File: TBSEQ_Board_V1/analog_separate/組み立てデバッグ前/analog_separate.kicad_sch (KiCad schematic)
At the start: 0 parts

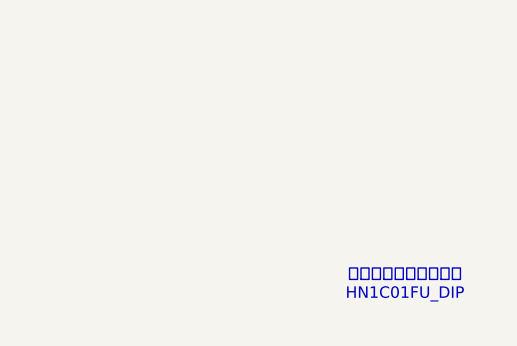
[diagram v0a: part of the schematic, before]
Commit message: analog_separate fix
実装してバグを修正
・VR6以外のボリュームの左右が逆なのを修正
・デュアルトランジスタをHN1C01FU-GRに変更
・VCA CA3080後の出力段のバイアス/増幅率等の設計ミスを修正
・入力信号のシルク位置が間違っているので修正
⇒それ以外は正常動作を確認済
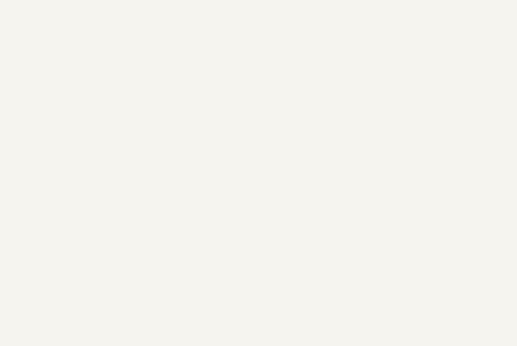
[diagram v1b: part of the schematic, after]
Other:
- note removed: "最終的にはこれに統一 HN1C01FU_DIP"
